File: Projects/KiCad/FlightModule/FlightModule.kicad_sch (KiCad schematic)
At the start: 60 parts, among them J1 Conn_01x08, J2 Conn_01x02_Pin, J3 Conn_01x02_Pin, J4 Conn_01x02_Pin, J5 Conn_01x02_Pin, J6 Conn_01x02_Pin, Q1 DTC143E, SW1 SW_Push, SW2 SW_Push, U1 MCP2562-E-P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

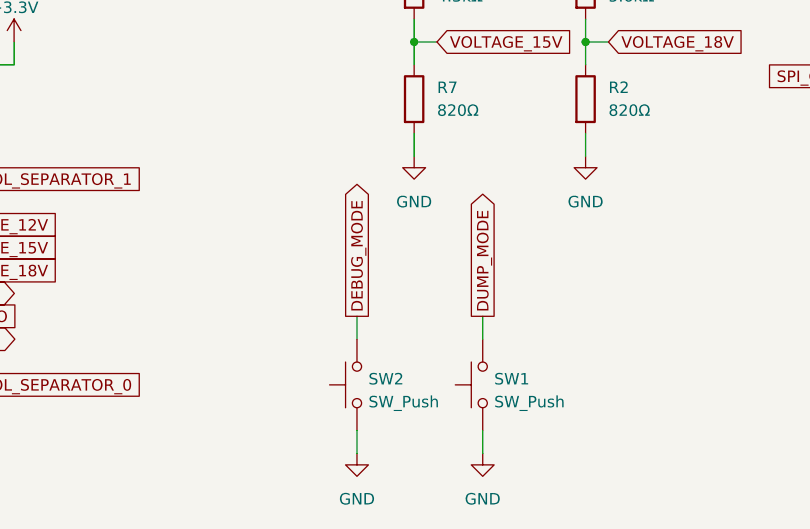
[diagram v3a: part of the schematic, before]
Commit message: スイッチをピアノスイッチに変更
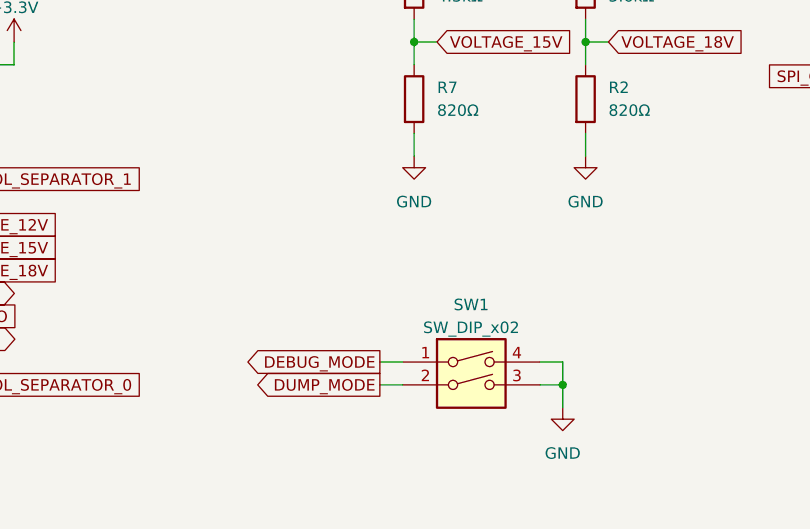
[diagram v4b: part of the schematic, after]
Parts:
- removed SW1, SW2: SW_Push, Button_Switch_THT:SW_PUSH_6mm, symbol Switch:SW_Push
- added SW1: SW_DIP_x02, Button_Switch_THT:SW_DIP_SPSTx02_Piano_10.8x6.64mm_W7.62mm_P2.54mm, symbol Switch:SW_DIP_x02
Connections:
- net DEBUG_MODE: now also SW1.1
- net DUMP_MODE: now also SW1.2
- net GND: now also SW1.3, SW1.4
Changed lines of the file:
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@@
   (junction (at 163.83 142.24) (diameter 0) (color 0 0 0 0)
   )
+  (junction (at 161.29 180.34) (diameter 0) (color 0 0 0 0)
+  )
   (no_connect (at 90.17 149.86))
   (no_connect (at 38.1 139.7))
@@
     (stroke (width 0) (type default))
   )
+  (wire (pts (xy 161.29 177.8) (xy 161.29 180.34))
+    (stroke (width 0) (type default))
+  )
   (wire (pts (xy 26.67 31.75) (xy 36.83 31.75))
     (stroke (width 0) (type default))
@@
     (stroke (width 0) (type default))
   )
-  (wire (pts (xy 138.43 185.42) (xy 138.43 187.96))
-    (stroke (width 0) (type default))
-  )
   (wire (pts (xy 210.82 140.97) (xy 208.28 140.97))
     (stroke (width 0) (type default))
@@
     (stroke (width 0) (type default))
   )
+  (wire (pts (xy 158.75 180.34) (xy 161.29 180.34))
+    (stroke (width 0) (type default))
+  )
   (wire (pts (xy 118.11 99.06) (xy 120.65 99.06))
     (stroke (width 0) (type default))
@@
     (stroke (width 0) (type default))
   )
+  (wire (pts (xy 161.29 180.34) (xy 161.29 182.88))
+    (stroke (width 0) (type default))
+  )
   (wire (pts (xy 220.98 151.13) (xy 220.98 153.67))
     (stroke (width 0) (type default))
@@
     (stroke (width 0) (type default))
   )
-  (wire (pts (xy 152.4 185.42) (xy 152.4 187.96))
-    (stroke (width 0) (type default))
-  )
   (wire (pts (xy 26.67 26.67) (xy 26.67 25.4))
     (stroke (width 0) (type default))
@@
     (stroke (width 0) (type default))
   )
-  (wire (pts (xy 138.43 172.72) (xy 138.43 175.26))
-    (stroke (width 0) (type default))
-  )
   (wire (pts (xy 264.16 81.28) (xy 266.7 81.28))
     (stroke (width 0) (type default))
@@
     (stroke (width 0) (type default))
   )
+  (wire (pts (xy 140.97 177.8) (xy 143.51 177.8))
+    (stroke (width 0) (type default))
+  )
+  (wire (pts (xy 158.75 177.8) (xy 161.29 177.8))
+    (stroke (width 0) (type default))
+  )
   (wire (pts (xy 38.1 160.02) (xy 40.64 160.02))
     (stroke (width 0) (type default))
@@
     (stroke (width 0) (type default))
   )
-  (wire (pts (xy 152.4 172.72) (xy 152.4 175.26))
-    (stroke (width 0) (type default))
-  )
   (wire (pts (xy 74.93 49.53) (xy 81.28 49.53))
     (stroke (width 0) (type default))
@@
     (stroke (width 0) (type default))
   )
+  (wire (pts (xy 140.97 180.34) (xy 143.51 180.34))
+    (stroke (width 0) (type default))
+  )
   (wire (pts (xy 198.12 146.05) (xy 200.66 146.05))
     (stroke (width 0) (type default))
@@
     )
   )
+  (global_label "DUMP_MODE" (shape output) (at 140.97 180.34 180) (fields_autoplaced)
+    (effects (font (size 1.27 1.27)) (justify right))
+    (property "Intersheetrefs" "${INTERSHEET_REFS}" (at 126.5738 180.34 0)
+      (effects (font (size 1.27 1.27)) (justify right) hide)
+    )
+  )
   (global_label "FLIGHT_MODE_BIT_2" (shape input) (at 154.94 43.18 90) (fields_autoplaced)
     (effects (font (size 1.27 1.27)) (justify left))
@@
     )
   )
+  (global_label "DEBUG_MODE" (shape output) (at 140.97 177.8 180) (fields_autoplaced)
+    (effects (font (size 1.27 1.27)) (justify right))
+    (property "Intersheetrefs" "${INTERSHEET_REFS}" (at 125.6062 177.8 0)
+      (effects (font (size 1.27 1.27)) (justify right) hide)
+    )
+  )
   (global_label "CAN_SEND_STATUS" (shape output) (at 38.1 149.86 180) (fields_autoplaced)
     (effects (font (size 1.27 1.27)) (justify right))
@@
     )
   )
-  (global_label "DUMP_MODE" (shape output) (at 152.4 172.72 90) (fields_autoplaced)
-    (effects (font (size 1.27 1.27)) (justify left))
-    (property "Intersheetrefs" "${INTERSHEET_REFS}" (at 152.4 158.3238 90)
-      (effects (font (size 1.27 1.27)) (justify left) hide)
-    )
-  )
   (global_label "SPI_MOSI" (shape input) (at 233.68 143.51 0) (fields_autoplaced)
     (effects (font (size 1.27 1.27)) (justify left))
@@
     )
   )
-  (global_label "DEBUG_MODE" (shape output) (at 138.43 172.72 90) (fields_autoplaced)
-    (effects (font (size 1.27 1.27)) (justify left))
-    (property "Intersheetrefs" "${INTERSHEET_REFS}" (at 138.43 157.3562 90)
-      (effects (font (size 1.27 1.27)) (justify left) hide)
-    )
-  )
   (global_label "VOLTAGE_18V" (shape input) (at 166.37 142.24 0) (fields_autoplaced)
     (effects (font (size 1.27 1.27)) (justify left))
@@
     )
   )
-  (symbol (lib_id "Switch:SW_Push") (at 138.43 180.34 90) (unit 1)
-    (in_bom yes) (on_board yes) (dnp no) (fields_autoplaced)
-    (property "Reference" "SW2" (at 139.7 179.705 90)
-      (effects (font (size 1.27 1.27)) (justify right))
-    )
-    (property "Value" "SW_Push" (at 139.7 182.245 90)
-      (effects (font (size 1.27 1.27)) (justify right))
-    )
-    (property "Footprint" "Button_Switch_THT:SW_PUSH_6mm" (at 133.35 180.34 0)
-      (effects (font (size 1.27 1.27)) hide)
-    )
-    (property "Datasheet" "~" (at 133.35 180.34 0)
-      (effects (font (size 1.27 1.27)) hide)
-    )
-    (pin "1")
-    (pin "2")
-    (instances
-      (project "FlightModule"
-        (path "/ea1ed597-7cd3-4340-902e-bdce8f2d7a62"
-          (reference "SW2") (unit 1)
-        )
-      )
-    )
-  )
   (symbol (lib_id "power:+5V") (at 95.25 139.7 0) (unit 1)
     (in_bom yes) (on_board yes) (dnp no) (fields_autoplaced)
@@
     )
   )
-  (symbol (lib_id "Switch:SW_Push") (at 152.4 180.34 90) (unit 1)
-    (in_bom yes) (on_board yes) (dnp no) (fields_autoplaced)
-    (property "Reference" "SW1" (at 153.67 179.705 90)
-      (effects (font (size 1.27 1.27)) (justify right))
-    )
-    (property "Value" "SW_Push" (at 153.67 182.245 90)
-      (effects (font (size 1.27 1.27)) (justify right))
-    )
-    (property "Footprint" "Button_Switch_THT:SW_PUSH_6mm" (at 147.32 180.34 0)
-      (effects (font (size 1.27 1.27)) hide)
-    )
-    (property "Datasheet" "~" (at 147.32 180.34 0)
-      (effects (font (size 1.27 1.27)) hide)
-    )
-    (pin "1")
-    (pin "2")
-    (instances
-      (project "FlightModule"
-        (path "/ea1ed597-7cd3-4340-902e-bdce8f2d7a62"
-          (reference "SW1") (unit 1)
-        )
-      )
-    )
-  )
   (symbol (lib_id "power:+5V") (at 78.74 25.4 0) (unit 1)
     (in_bom yes) (on_board yes) (dnp no) (fields_autoplaced)
@@
     )
   )
-  (symbol (lib_id "power:GND") (at 152.4 187.96 0) (mirror y) (unit 1)
-    (in_bom yes) (on_board yes) (dnp no) (fields_autoplaced)
-    (property "Reference" "#PWR027" (at 152.4 194.31 0)
-      (effects (font (size 1.27 1.27)) hide)
-    )
-    (property "Value" "GND" (at 152.4 193.04 0)
-      (effects (font (size 1.27 1.27)))
-    )
-    (property "Footprint" "" (at 152.4 187.96 0)
-      (effects (font (size 1.27 1.27)) hide)
-    )
-    (property "Datasheet" "" (at 152.4 187.96 0)
-      (effects (font (size 1.27 1.27)) hide)
-    )
-    (pin "1")
-    (instances
-      (project "FlightModule"
-        (path "/ea1ed597-7cd3-4340-902e-bdce8f2d7a62"
-          (reference "#PWR027") (unit 1)
-        )
-      )
-    )
-  )
   (symbol (lib_id "Connector:Conn_01x02_Pin") (at 100.33 104.14 0) (mirror x) (unit 1)
     (in_bom yes) (on_board yes) (dnp no)
@@
     )
   )
+  (symbol (lib_id "power:GND") (at 161.29 182.88 0) (mirror y) (unit 1)
+    (in_bom yes) (on_board yes) (dnp no) (fields_autoplaced)
+    (property "Reference" "#PWR025" (at 161.29 189.23 0)
+      (effects (font (size 1.27 1.27)) hide)
+    )
+    (property "Value" "GND" (at 161.29 187.96 0)
+      (effects (font (size 1.27 1.27)))
+    )
+    (property "Footprint" "" (at 161.29 182.88 0)
+      (effects (font (size 1.27 1.27)) hide)
+    )
+    (property "Datasheet" "" (at 161.29 182.88 0)
+      (effects (font (size 1.27 1.27)) hide)
+    )
+    (pin "1")
+    (instances
+      (project "FlightModule"
+        (path "/ea1ed597-7cd3-4340-902e-bdce8f2d7a62"
+          (reference "#PWR025") (unit 1)
+        )
+      )
+    )
+  )
   (symbol (lib_id "power:GND") (at 218.44 58.42 0) (mirror y) (unit 1)
     (in_bom yes) (on_board yes) (dnp no) (fields_autoplaced)
@@
     )
   )
+  (symbol (lib_id "Switch:SW_DIP_x02") (at 151.13 180.34 0) (unit 1)
+    (in_bom yes) (on_board yes) (dnp no) (fields_autoplaced)
+    (property "Reference" "SW1" (at 151.13 171.45 0)
+      (effects (font (size 1.27 1.27)))
+    )
+    (property "Value" "SW_DIP_x02" (at 151.13 173.99 0)
+      (effects (font (size 1.27 1.27)))
+    )
+    (property "Footprint" "Button_Switch_THT:SW_DIP_SPSTx02_Piano_10.8x6.64mm_W7.62mm_P2.54mm" (at 151.13 180.34 0)
+      (effects (font (size 1.27 1.27)) hide)
+    )
+    (property "Datasheet" "~" (at 151.13 180.34 0)
+      (effects (font (size 1.27 1.27)) hide)
+    )
+    (pin "1")
+    (pin "2")
+    (pin "3")
+    (pin "4")
+    (instances
+      (project "FlightModule"
+        (path "/ea1ed597-7cd3-4340-902e-bdce8f2d7a62"
+          (reference "SW1") (unit 1)
+        )
+      )
+    )
+  )
   (symbol (lib_id "Device:LED") (at 134.62 59.69 90) (unit 1)
     (in_bom yes) (on_board yes) (dnp no)
@@
         )
       )
-    )
-  )
-  (symbol (lib_id "power:GND") (at 138.43 187.96 0) (mirror y) (unit 1)
-    (in_bom yes) (on_board yes) (dnp no) (fields_autoplaced)
-    (property "Reference" "#PWR025" (at 138.43 194.31 0)
-      (effects (font (size 1.27 1.27)) hide)
-    )
-    (property "Value" "GND" (at 138.43 193.04 0)
-      (effects (font (size 1.27 1.27)))
-    )
-    (property "Footprint" "" (at 138.43 187.96 0)
-      (effects (font (size 1.27 1.27)) hide)
-    )
-    (property "Datasheet" "" (at 138.43 187.96 0)
-      (effects (font (size 1.27 1.27)) hide)
-    )
-    (pin "1")
-    (instances
-      (project "FlightModule"
-        (path "/ea1ed597-7cd3-4340-902e-bdce8f2d7a62"
-          (reference "#PWR025") (unit 1)
-        )
-      )

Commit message: 変圧基板を追加
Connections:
- net VOLTAGE_15V renamed VOLTAGE_BATT
- net VOLTAGE_18V renamed VOLTAGE_VSW
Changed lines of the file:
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@@
     )
   )
-  (global_label "VOLTAGE_18V" (shape input) (at 90.17 167.64 0) (fields_autoplaced)
-    (effects (font (size 1.27 1.27)) (justify left))
-    (property "Intersheetrefs" "${INTERSHEET_REFS}" (at 105.4734 167.64 0)
+  (global_label "VOLTAGE_VSW" (shape input) (at 90.17 167.64 0) (fields_autoplaced)
+    (effects (font (size 1.27 1.27)) (justify left))
+    (property "Intersheetrefs" "${INTERSHEET_REFS}" (at 105.7153 167.64 0)
       (effects (font (size 1.27 1.27)) (justify left) hide)
     )
@@
     )
   )
-  (global_label "VOLTAGE_15V" (shape input) (at 147.32 142.24 0) (fields_autoplaced)
-    (effects (font (size 1.27 1.27)) (justify left))
-    (property "Intersheetrefs" "${INTERSHEET_REFS}" (at 162.6234 142.24 0)
+  (global_label "VOLTAGE_BATT" (shape input) (at 147.32 142.24 0) (fields_autoplaced)
+    (effects (font (size 1.27 1.27)) (justify left))
+    (property "Intersheetrefs" "${INTERSHEET_REFS}" (at 163.4096 142.24 0)
       (effects (font (size 1.27 1.27)) (justify left) hide)
     )
@@
     )
   )
-  (global_label "VOLTAGE_15V" (shape input) (at 90.17 165.1 0) (fields_autoplaced)
-    (effects (font (size 1.27 1.27)) (justify left))
-    (property "Intersheetrefs" "${INTERSHEET_REFS}" (at 105.4734 165.1 0)
+  (global_label "VOLTAGE_BATT" (shape input) (at 90.17 165.1 0) (fields_autoplaced)
+    (effects (font (size 1.27 1.27)) (justify left))
+    (property "Intersheetrefs" "${INTERSHEET_REFS}" (at 106.2596 165.1 0)
       (effects (font (size 1.27 1.27)) (justify left) hide)
     )
@@
     )
   )
-  (global_label "VOLTAGE_18V" (shape input) (at 166.37 142.24 0) (fields_autoplaced)
-    (effects (font (size 1.27 1.27)) (justify left))
-    (property "Intersheetrefs" "${INTERSHEET_REFS}" (at 181.6734 142.24 0)
-      (effects (font (size 1.27 1.27)) (justify left) hide)
-    )
+  (global_label "VOLTAGE_VSW" (shape input) (at 166.37 142.24 0) (fields_autoplaced)
+    (effects (font (size 1.27 1.27)) (justify left))
+    (property "Intersheetrefs" "${INTERSHEET_REFS}" (at 181.9153 142.24 0)
+      (effects (font (size 1.27 1.27)) (justify left) hide)
+    )
